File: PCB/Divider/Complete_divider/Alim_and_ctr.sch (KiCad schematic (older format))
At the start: 9 parts, among them U1 SFH617A-1

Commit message: Reorganize
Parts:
- added C?: 2500pF 15 kV, Capacitor_THT:C_Rect_L13.0mm_W8.0mm_P10.00mm_FKS3_FKP3_MKS4, symbol Device:C
- added C?: 4700pF 10kV, Capacitor_THT:C_Rect_L13.0mm_W8.0mm_P10.00mm_FKS3_FKP3_MKS4, symbol Device:C
- added E29, E30, J1, J? (x6): Electrode, Connector_Pin:Pin_D1.0mm_L10.0mm, symbol Connector:Conn_01x01_Female
- added HT1, HT2: HT, symbol power:HT
- added R28, R29, R30: 10M, Resistor_SMD:R_1206_3216Metric, symbol Device:R
- renumbered C1 to C11, C2 to C12, C3 to C13, R60 to R101, R61 to R102, R62 to R103, R59 to R104, RV1 to RV11, U1 to U11
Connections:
- net labels added: DESOLVATION
- wire segments 24 -> 48
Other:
- note added: "15kV\n"
- note added: "5kV\n"
- moved on the sheet: C11, C12, C13, R104

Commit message: Most parts completed
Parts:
- removed R28, R30: 10M, Resistor_SMD:R_1206_3216Metric, symbol Device:R
- added E29, E31: Electrode out, Connector_Pin:Pin_D1.0mm_L10.0mm, symbol Connector:Conn_01x01_Female
- E28: renamed from E29; value Electrode -> Electrode in
- E30: value Electrode -> Electrode out
- renumbered RV11 to R29, R29 to R30
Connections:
- wire segments 48 -> 52
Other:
- moved on the sheet: E30, R29, R30
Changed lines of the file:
@@
 	1    0    0    -1
 $EndComp
-$Comp
-L Device:R_POT RV11
-U 1 1 5E6EEFD6
-P 3450 2650
-F 0 "RV11" H 3380 2696 50  0000 R CNN
-F 1 "100M" H 3380 2605 50  0000 R CNN
-F 2 "Potentiometer_THT:Potentiometer_ACP_CA14-H4_Horizontal" H 3450 2650 50  0001 C CNN
-F 3 "~" H 3450 2650 50  0001 C CNN
-	1    3450 2650
-	1    0    0    -1
-$EndComp
-Wire Wire Line
-	3450 2800 3450 2900
 Connection ~ 3450 2900
 NoConn ~ 4000 3800
@@
 	3600 3200 4000 3200
 Wire Wire Line
-	3600 2650 3600 3200
-Wire Wire Line
 	3450 2900 3450 3600
 Wire Wire Line
 	3450 3800 3450 4300
-Text GLabel 4550 5350 2    50   Output ~ 0
-DRIFTTUBE
 Connection ~ 4950 3200
 Wire Wire Line
@@
 Wire Wire Line
 	3450 4700 5200 4700
-$Comp
-L Device:R R30
-U 1 1 5E6A649D
-P 3800 5350
-F 0 "R30" V 3593 5350 50  0000 C CNN
-F 1 "10M" V 3684 5350 50  0000 C CNN
-F 2 "Resistor_SMD:R_1206_3216Metric" V 3730 5350 50  0001 C CNN
-F 3 "~" H 3800 5350 50  0001 C CNN
-	1    3800 5350
-	0    1    1    0
-$EndComp
-Wire Wire Line
-	3450 4700 3450 5350
-Wire Wire Line
-	3450 5350 3650 5350
 Connection ~ 3450 4700
 Wire Wire Line
-	3950 5350 4200 5350
-$Comp
-L Connector:Conn_01x01_Female E30
-U 1 1 5E6A87F4
-P 4200 5550
-F 0 "E30" V 4200 5750 50  0000 R CNN
-F 1 "Electrode" V 4100 5950 50  0000 R CNN
-F 2 "Connector_Pin:Pin_D1.0mm_L10.0mm" H 4200 5550 50  0001 C CNN
-F 3 "~" H 4200 5550 50  0001 C CNN
-	1    4200 5550
-	0    1    1    0
-$EndComp
-Connection ~ 4200 5350
-Wire Wire Line
-	4200 5350 4550 5350
-Wire Wire Line
 	2750 2300 2750 2350
-Wire Wire Line
-	2750 2350 3150 2350
 Connection ~ 2750 2350
 $Comp
-L Connector:Conn_01x01_Female E29
+L Connector:Conn_01x01_Female E28
 U 1 1 5E6A298B
 P 2750 2100
-F 0 "E29" V 2700 2050 50  0000 R CNN
-F 1 "Electrode" V 2600 2050 50  0000 R CNN
+F 0 "E28" V 2700 2050 50  0000 R CNN
+F 1 "Electrode in" V 2600 2050 50  0000 R CNN
 F 2 "Connector_Pin:Pin_D1.0mm_L10.0mm" H 2750 2100 50  0001 C CNN
 F 3 "~" H 2750 2100 50  0001 C CNN
@@
 	0    -1   -1   0
 $EndComp
-Wire Wire Line
-	2600 2350 2750 2350
-$Comp
-L Device:R R29
-U 1 1 5E6A197B
-P 3300 2350
-F 0 "R29" V 3093 2350 50  0000 C CNN
-F 1 "10M" V 3184 2350 50  0000 C CNN
-F 2 "Resistor_SMD:R_1206_3216Metric" V 3230 2350 50  0001 C CNN
-F 3 "~" H 3300 2350 50  0001 C CNN
-	1    3300 2350
-	0    1    1    0
-$EndComp
-$Comp
-L Device:R R28
-U 1 1 5E6A0CFA
-P 2450 2350
-F 0 "R28" V 2243 2350 50  0000 C CNN
-F 1 "10M" V 2334 2350 50  0000 C CNN
-F 2 "Resistor_SMD:R_1206_3216Metric" V 2380 2350 50  0001 C CNN
-F 3 "~" H 2450 2350 50  0001 C CNN
-	1    2450 2350
-	0    1    1    0
-$EndComp
-Wire Wire Line
-	2050 2350 2300 2350
 Text GLabel 2050 2350 0    50   Input ~ 0
 TRI-STATE
-Wire Wire Line
-	3450 2350 3450 2500
 $Comp
 L Connector:Conn_01x01_Female J1
@@
 	7400 5500 7500 5500
 Connection ~ 7400 5250
+Wire Wire Line
+	2750 2350 3450 2350
+Text GLabel 3600 6250 2    50   Output ~ 0
+DRIFTTUBE
+Wire Wire Line
+	3450 6250 3600 6250
+$Comp
+L Connector:Conn_01x01_Female E31
+U 1 1 5E686FBB
+P 3850 5950
+F 0 "E31" H 3850 6050 50  0000 R CNN
+F 1 "Electrode out" H 4050 5900 50  0000 R CNN
+F 2 "Connector_Pin:Pin_D1.0mm_L10.0mm" H 3850 5950 50  0001 C CNN
+F 3 "~" H 3850 5950 50  0001 C CNN
+	1    3850 5950
+	1    0    0    -1
+$EndComp
+Wire Wire Line
+	3650 5950 3450 5950
+Connection ~ 3450 5950
+Wire Wire Line
+	3450 5950 3450 6250
+Wire Wire Line
+	2050 2350 2750 2350
+Wire Wire Line
+	3450 2700 3450 2750
+Wire Wire Line
+	3600 2550 3600 3200
+Wire Wire Line
+	3450 2350 3450 2400
+$Comp
+L Device:R_POT R29
+U 1 1 5E6EEFD6
+P 3450 2550
+F 0 "R29" H 3380 2596 50  0000 R CNN
+F 1 "100M" H 3380 2505 50  0000 R CNN
+F 2 "Potentiometer_THT:Potentiometer_ACP_CA14-H4_Horizontal" H 3450 2550 50  0001 C CNN
+F 3 "~" H 3450 2550 50  0001 C CNN
+	1    3450 2550
+	1    0    0    -1
+$EndComp
+$Comp
+L Connector:Conn_01x01_Female E29
+U 1 1 5E65A357
+P 3850 2750
+F 0 "E29" H 3850 2850 50  0000 R CNN
+F 1 "Electrode out" H 4200 2700 50  0000 R CNN
+F 2 "Connector_Pin:Pin_D1.0mm_L10.0mm" H 3850 2750 50  0001 C CNN
+F 3 "~" H 3850 2750 50  0001 C CNN
+	1    3850 2750
+	1    0    0    -1
+$EndComp
+Wire Wire Line
+	3450 2750 3650 2750
+Connection ~ 3450 2750
+Wire Wire Line
+	3450 2750 3450 2900
+Wire Wire Line
+	3450 4700 3450 5150
+$Comp
+L Connector:Conn_01x01_Female E30
+U 1 1 5E6A87F4
+P 3900 5150
+F 0 "E30" H 3900 5250 50  0000 R CNN
+F 1 "Electrode out" H 4100 5100 50  0000 R CNN
+F 2 "Connector_Pin:Pin_D1.0mm_L10.0mm" H 3900 5150 50  0001 C CNN
+F 3 "~" H 3900 5150 50  0001 C CNN
+	1    3900 5150
+	1    0    0    -1
+$EndComp
+Wire Wire Line
+	3700 5150 3450 5150
+Wire Wire Line
+	3450 5650 3450 5950
+$Comp
+L Device:R R30
+U 1 1 5E6A197B
+P 3450 5500
+F 0 "R30" H 3300 5550 50  0000 C CNN
+F 1 "10M" H 3300 5450 50  0000 C CNN
+F 2 "Resistor_SMD:R_1206_3216Metric" V 3380 5500 50  0001 C CNN
+F 3 "~" H 3450 5500 50  0001 C CNN
+	1    3450 5500
+	-1   0    0    1
+$EndComp
+Wire Wire Line
+	3450 5350 3450 5150
+Connection ~ 3450 5150
 $EndSCHEMATC

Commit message: Implementation of the HV sources footprints and schems
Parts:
- removed C?: 2500pF 15 kV, Capacitor_THT:C_Rect_L13.0mm_W8.0mm_P10.00mm_FKS3_FKP3_MKS4, symbol Device:C
- removed C?: 4700pF 10kV, Capacitor_THT:C_Rect_L13.0mm_W8.0mm_P10.00mm_FKS3_FKP3_MKS4, symbol Device:C
- removed HT1, HT2: HT, symbol power:HT
- removed J? (x3): Electrode, Connector_Pin:Pin_D1.0mm_L10.0mm, symbol Connector:Conn_01x01_Female
- added C?: 4700pF 10kV, Capacitor_THT:C_Rect_L13.0mm_W8.0mm_P10.00mm_FKS3_FKP3_MKS4, symbol Device:C
- added C?: 2500pF 15 kV, Capacitor_THT:C_Rect_L13.0mm_W8.0mm_P10.00mm_FKS3_FKP3_MKS4, symbol Device:C
- added HT1 (x2), HT2 (x2): HT, symbol power:HT
- added HV1: 15A, symbol HV_source:15A
- added HV1: G40, symbol HV_source:G40
- added J2, J3: HV out, Connector_Pin:Pin_D1.0mm_L10.0mm, symbol Connector:Conn_01x01_Female
- added J?: Alim1, symbol Connector:Conn_01x02_Male
- added J?: Alim2, symbol Connector:Conn_01x02_Male
- added POT1: R_POT, symbol Device:R_POT
- J1: value Electrode -> HV out
- gave numbers to parts that had none: 3
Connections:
- net labels added: COUNTER_ELECTRODE, LAST_ELECTRODE, NEEDLE
- net labels removed: DESOLVATION
- wire segments 52 -> 66
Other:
- note added: "Pinouts for Electrodes\n"
- note added: "Pinouts for HV\n"
- note removed: "15kV\n"
- note removed: "5kV\n"
- moved on the sheet: C11, C12, C13, E28, E29, E30, E31, J4, J5, J6, R101, R102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

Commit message: Small modifications
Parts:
- removed HT1 (x2), HT2 (x2): HT, symbol power:HT
- removed J4, J5, J6: Electrode, Connector_Pin:Pin_D1.0mm_L10.0mm, symbol Connector:Conn_01x01_Female
- added J? (x3): Pinout, Connector_Pin:Pin_D1.0mm_L10.0mm, symbol Connector:Conn_01x01_Female
- R?: renamed from R29; value 100M -> 10M
- renumbered C13 to C?, C11 to C?, C12 to C?, E29 to E?, E30 to E?, HV1 to HV?, E31 to J?, E28 to J?, J1 to J?, J2 to J?, J3 to J?, POT1 to POT?, R103 to R?, R102 to R?, R30 to R?, R104 to R?, R101 to R?, U11 to U?
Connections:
- net labels added: 15kV, 19kV, Electrode_in, Electrode_out, Middle_electrode1, Middle_electrode2, Needle, Pwr_out
- wire segments 66 -> 86
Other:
- note added: "Pinouts for power HV\n"
- note removed: "Pinouts for HV\n"
- moved on the sheet: E?, J?

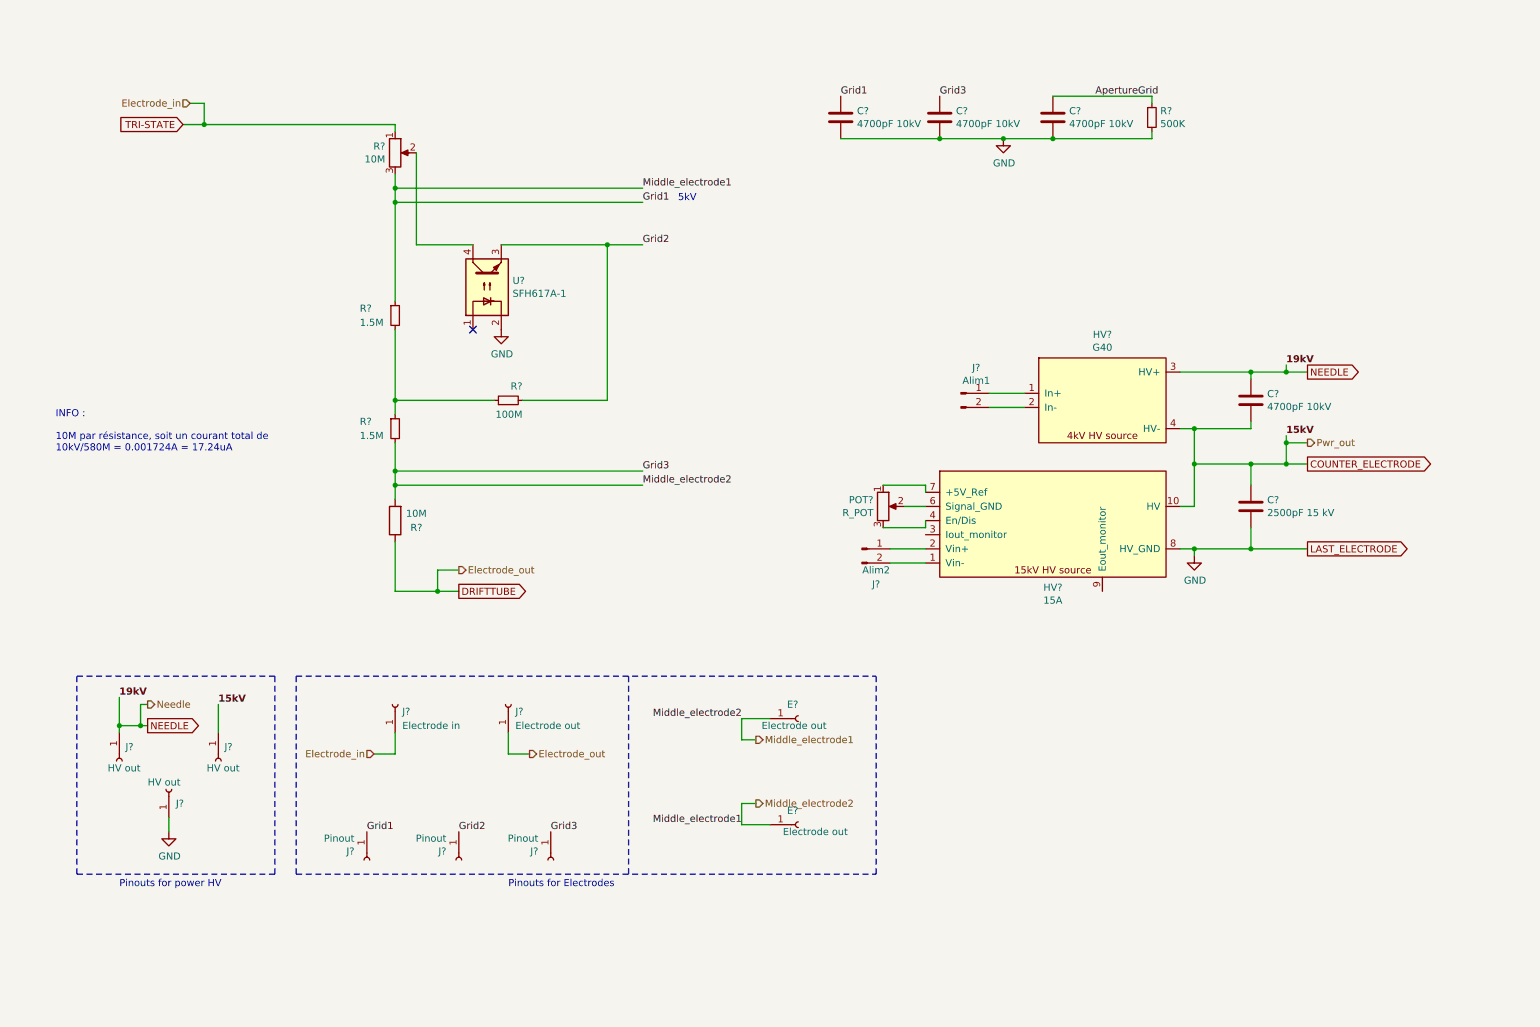
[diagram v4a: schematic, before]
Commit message: Implementing MCU
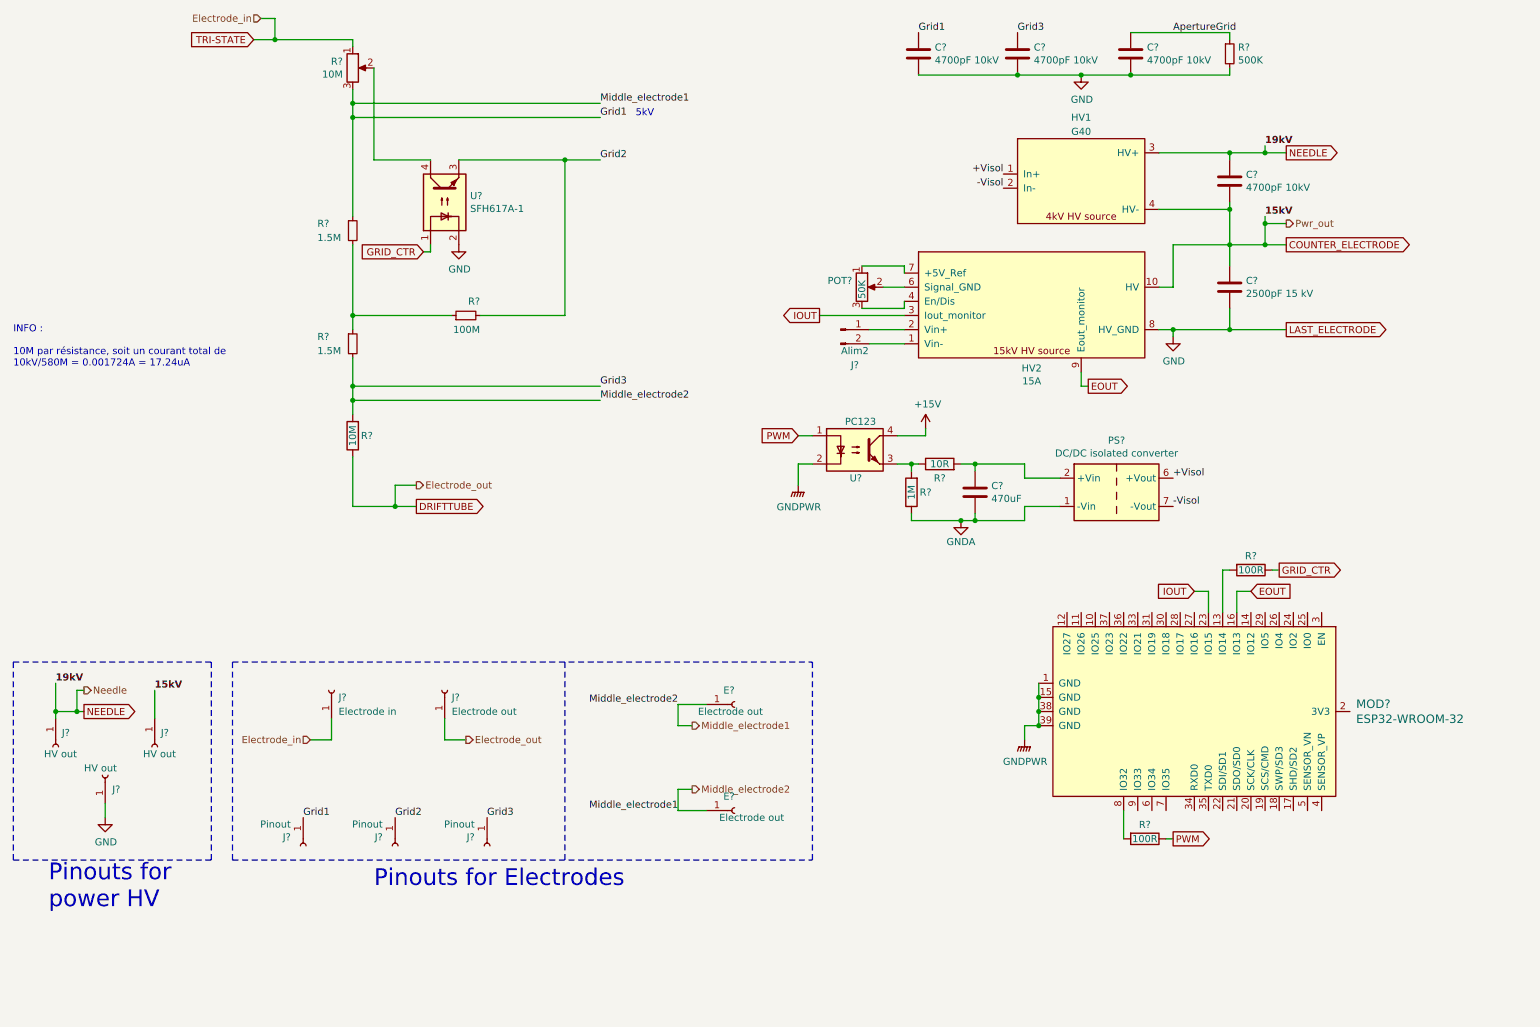
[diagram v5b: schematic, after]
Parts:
- removed J?: Alim1, symbol Connector:Conn_01x02_Male
- added C?: 470uF, Capacitor_THT:C_Rect_L13.0mm_W8.0mm_P10.00mm_FKS3_FKP3_MKS4, symbol Device:C
- added MOD?: ESP32-WROOM-32, digikey-footprints:ESP32-WROOM-32D, symbol dk_RF-Transceiver-Modules:ESP32-WROOM-32
- added PS?: DC/DC isolated converter, Converter_DCDC:Converter_DCDC_XP_POWER-ITXxxxxSA_THT, symbol Converter_DCDC:ITX0503SA-H
- added R? (x2): 100R, symbol Device:R
- added R?: 1M, symbol Device:R
- added R?: 10R, symbol Device:R
- added U?: PC123, Package_DIP:DIP-4_W7.62mm, symbol Isolator:SFH617A-1
- POT?: value R_POT -> 50K
- gave numbers to parts that had none: 2
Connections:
- net GRID_CTR: now reaches U?.1
- net GRID_CTR: now also R?.1
- net IOUT: now reaches HV2.3 (Iout_monitor)
- net IOUT: now also MOD?.23 (IO15)
- net EOUT: now reaches HV2.9 (Eout_monitor)
- net EOUT: now also MOD?.16 (IO13)
- net +Visol: now reaches HV1.1 (In+)
- net +Visol: now also PS?.6 (+Vout)
- net -Visol: now reaches HV1.2 (In-)
- net -Visol: now also PS?.7 (-Vout)
- new net: MOD?.13 (IO14), R?.2
- new net: MOD?.8 (IO32), R?.2
- new net: R?.1, R?.2, U?.3
- new net: C?.1, PS?.2 (+Vin), R?.2
- new net +15V: U?.4
- new net GNDA: C?.2, PS?.1 (-Vin), R?.1
- new net GNDPWR: MOD?.1 (GND), MOD?.15 (GND), MOD?.38 (GND), MOD?.39 (GND), U?.2
- new net PWM: R?.1, U?.1
- no-connect marks 1 -> 0
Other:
- note added: "Pinouts for \npower HV\n"
- note removed: "Pinouts for power HV\n"
- moved on the sheet: C?, E?, J?, POT?, R?, U?

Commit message: Labelling/ordering stuff
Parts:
- removed R? (x2): 1.5M, Resistor_SMD:R_1206_3216Metric, symbol Device:R_Small
- added R? (x2): 1.5M, symbol Device:R
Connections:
- net Middle_electrode1: now also R?.1, R?.2
- net at R?.1: now also R?.1, R?.2
- net GRID_CTR renamed GRID_CTRL
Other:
- note added: "MCU\n"
- note added: "POWER"
- note added: "PWM \n"
- moved on the sheet: C?, E?, J?, MOD?, POT?, PS?, R?, U?

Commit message: updates
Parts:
- removed MOD?: ESP32-WROOM-32, digikey-footprints:ESP32-WROOM-32D, symbol dk_RF-Transceiver-Modules:ESP32-WROOM-32
- removed R?: 100M, Resistor_SMD:R_1206_3216Metric, symbol Device:R_Small
- added Cboost: 100nF, symbol Device:C_Small
- added Cin: 22uF, symbol Device:CP1_Small
- added Cout: 47uF, symbol Device:C_Small
- added J?: Low voltage in, symbol Connector:Conn_01x02_Male
- added L1: 4.7uH, symbol Device:L_Small
- added Q?: BC337, digikey-footprints:TO-39-3, symbol dk_Transistors-Bipolar-BJT-RF:2N5109
- added R?: 100M, symbol Device:R
- added Rfbb: 10k, Resistor_SMD:R_1206_3216Metric, symbol Device:R_Small
- added Rfbt: 73.2k, Resistor_SMD:R_1206_3216Metric, symbol Device:R_Small
- added U?: Lolin32, symbol symbols:Lolin32
- added U?: TPS561208, Package_TO_SOT_SMD:SOT-23-6, symbol Regulator_Switching:TPS562200
- R?: value 10R -> 10R 1W
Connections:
- net GNDPWR is gone; now on net GNDA: U?.2
- net +15V: now also Cin.1, J?.1 (Pin_1), Q?.3 (C), U?.3 (VIN), U?.5 (EN)
- net EOUT: now also U?.11 (A17/27)
- net GNDA: now also Cin.2, Cout.2, J?.2 (Pin_2), Rfbb.2, U?.1 (GND), U?.16 (GND), U?.17 (GND), U?.34 (GND)
- net Grid2: now also R?.1
- net IOUT: now also U?.13 (A15/12)
- net at R?.1, R?.2: now also R?.2
- net at R?.2: now also U?.12 (A16/14)
- net at R?.2: now also U?.30 (17)
- net at R?.1, R?.2: now also Q?.1 (E); no longer U?.3
- new net: Q?.2 (B), U?.3
- new net: Cboost.2, U?.2 (SW)
- new net: Rfbb.1, Rfbt.2, U?.4 (VFB)
- new net: Cboost.1, L1.2, U?.6 (VBST)
- new net: Cout.1, L1.1, Rfbt.1
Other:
- note added: "ALIM\n"
- moved on the sheet: C?, E?, J?, POT?, PS?, R?, U?
